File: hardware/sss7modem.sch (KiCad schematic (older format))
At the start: 30 parts, among them IC1 MCP2551-I/SN, IC2 LTV-352T, IC3 LTV-352T, K1 CONN_3, P1 CONN_4, U1 SIM1-0505, U2 74HCT125

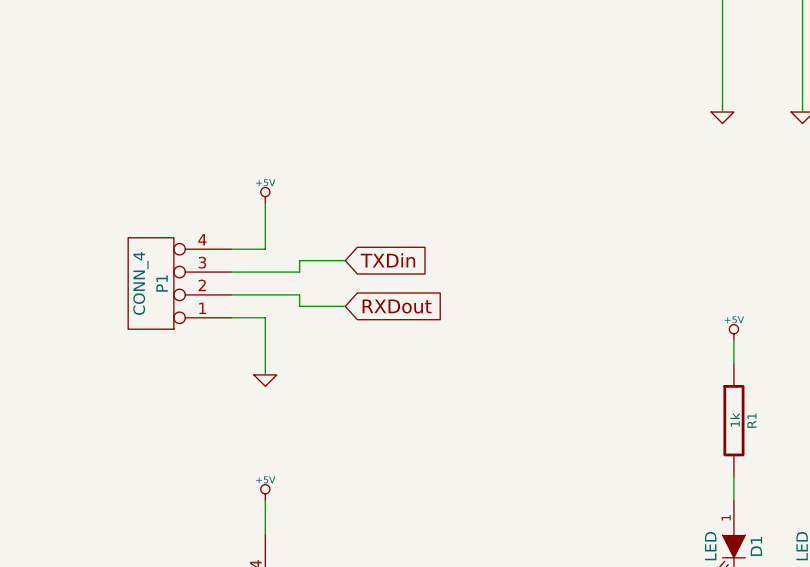
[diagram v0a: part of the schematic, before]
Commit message: First draft for the split ground pcb
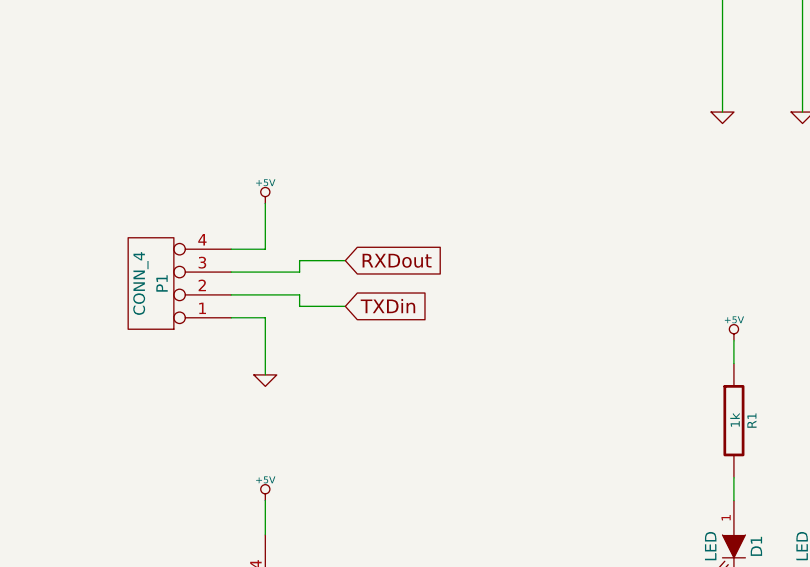
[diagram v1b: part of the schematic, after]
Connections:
- net RXDout: now also P1.3 (P3); no longer P1.2 (P2)
- net TXDin: now also P1.2 (P2); no longer P1.3 (P3)
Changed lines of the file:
@@
 Wire Wire Line
 	2900 3600 3100 3600
+Text GLabel 3100 3600 2    60   Input ~ 0
+TXDin
 Text GLabel 3100 3400 2    60   Input ~ 0
-TXDin
-Text GLabel 3100 3600 2    60   Input ~ 0
 RXDout
 Text Notes 7550 900  0    197  ~ 0

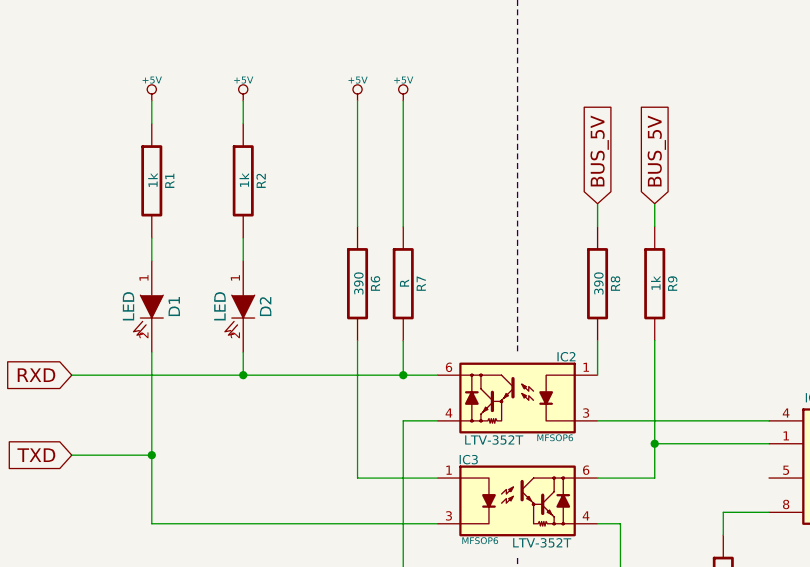
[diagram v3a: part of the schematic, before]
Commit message: Added missing resistor value
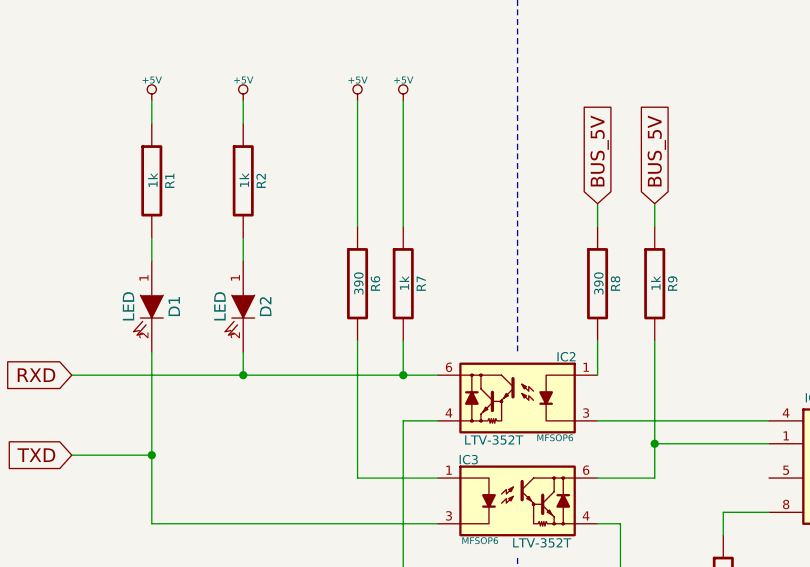
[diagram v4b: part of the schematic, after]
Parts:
- R7: value R -> 1k
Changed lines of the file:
@@
 Sheet 1 1
 Title "Seidenstrasse Signaling System 7 Modem"
-Date "26 may 2015"
+Date "22 jun 2015"
 Rev "1.0"
-Comp "Telebørken"
+Comp "Chaos Seidenstrasse Werke Kaiserslautern"
 Comment1 ""
 Comment2 ""
@@
 P 5900 4550
 F 0 "R7" V 5980 4550 40  0000 C CNN
-F 1 "R" V 5907 4551 40  0000 C CNN
+F 1 "1k" V 5907 4551 40  0000 C CNN
 F 2 "~" V 5830 4550 30  0000 C CNN
 F 3 "~" H 5900 4550 30  0000 C CNN

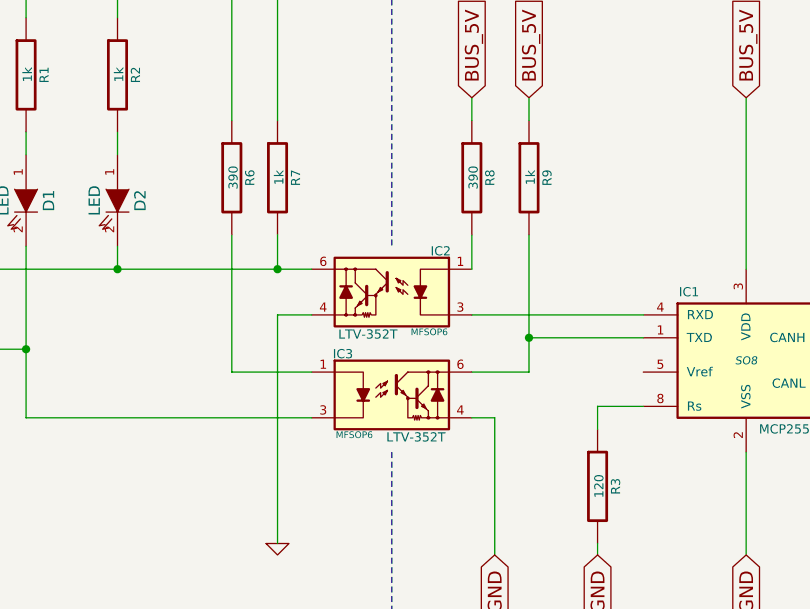
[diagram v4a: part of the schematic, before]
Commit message: Changes optocouplers to something faster. fixes #1
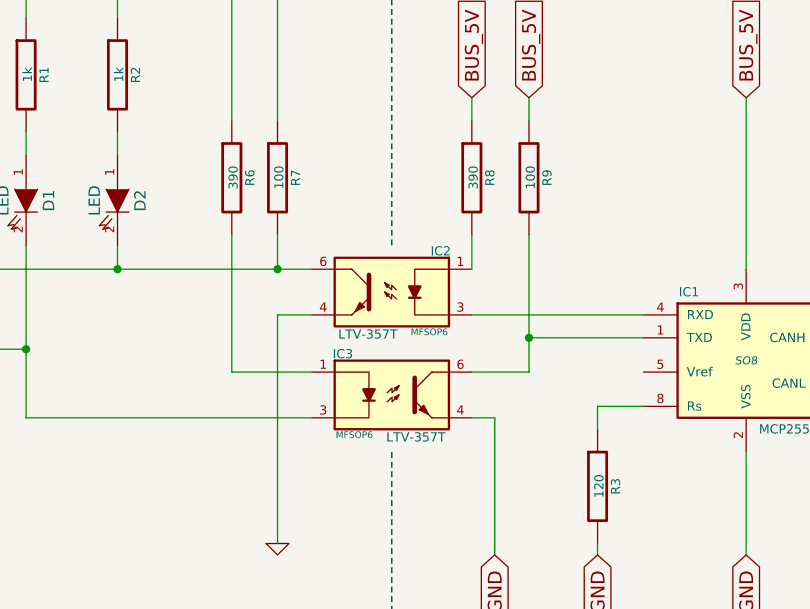
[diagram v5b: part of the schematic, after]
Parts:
- removed IC2, IC3: LTV-352T, MFSOP6, symbol LTV-352T
- added IC2, IC3: LTV-357T, MFSOP6, symbol LTV-357T
- R7, R9: value 1k -> 100
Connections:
- net BUS_GND: now also IC3.4
- net GND: now also IC2.4
- net RXD: now also IC2.6
- net TXD: now also IC3.3
- net at IC1.1 (TXD), R9.2: now also IC3.6
- net at IC1.4 (RXD): now also IC2.3
- net at R6.2: now also IC3.1
- net at R8.2: now also IC2.1
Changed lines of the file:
@@
 Sheet 1 1
 Title "Seidenstrasse Signaling System 7 Modem"
-Date "22 jun 2015"
+Date "8 jul 2015"
 Rev "1.0"
 Comp "Chaos Seidenstrasse Werke Kaiserslautern"
@@
 	1    0    0    -1
 $EndComp
-$Comp
-L LTV-352T IC3
-U 1 1 555DB3D8
-P 6400 5500
-F 0 "IC3" H 6186 5679 40  0000 C CNN
-F 1 "LTV-352T" H 6505 5315 40  0000 C CNN
-F 2 "MFSOP6" H 6236 5325 29  0000 C CNN
-F 3 "~" H 6400 5500 60  0000 C CNN
-	1    6400 5500
-	1    0    0    -1
-$EndComp
-$Comp
-L LTV-352T IC2
-U 1 1 555DB3E7
-P 6400 5050
-F 0 "IC2" H 6186 5229 40  0000 C CNN
-F 1 "LTV-352T" H 6505 4865 40  0000 C CNN
-F 2 "MFSOP6" H 6236 4875 29  0000 C CNN
-F 3 "~" H 6400 5050 60  0000 C CNN
-	1    6400 5050
-	-1   0    0    -1
-$EndComp
 Text GLabel 7950 4200 1    60   Input ~ 0
 BUS_5V
@@
 P 7000 4550
 F 0 "R9" V 7080 4550 40  0000 C CNN
-F 1 "1k" V 7007 4551 40  0000 C CNN
+F 1 "100" V 7007 4551 40  0000 C CNN
 F 2 "~" V 6930 4550 30  0000 C CNN
 F 3 "~" H 7000 4550 30  0000 C CNN
@@
 P 5900 4550
 F 0 "R7" V 5980 4550 40  0000 C CNN
-F 1 "1k" V 5907 4551 40  0000 C CNN
+F 1 "100" V 5907 4551 40  0000 C CNN
 F 2 "~" V 5830 4550 30  0000 C CNN
 F 3 "~" H 5900 4550 30  0000 C CNN
@@
 EndData
 $EndBitmap
+$Comp
+L LTV-357T IC3
+U 1 1 559CDFCD
+P 6400 5500
+F 0 "IC3" H 6186 5679 40  0000 C CNN
+F 1 "LTV-357T" H 6505 5315 40  0000 C CNN
+F 2 "MFSOP6" H 6236 5325 29  0000 C CNN
+F 3 "~" H 6400 5500 60  0000 C CNN
+	1    6400 5500
+	1    0    0    -1
+$EndComp
+$Comp
+L LTV-357T IC2
+U 1 1 559CDFF5
+P 6400 5050
+F 0 "IC2" H 6186 5229 40  0000 C CNN
+F 1 "LTV-357T" H 6505 4865 40  0000 C CNN
+F 2 "MFSOP6" H 6236 4875 29  0000 C CNN
+F 3 "~" H 6400 5050 60  0000 C CNN
+	1    6400 5050
+	-1   0    0    -1
+$EndComp
 $EndSCHEMATC

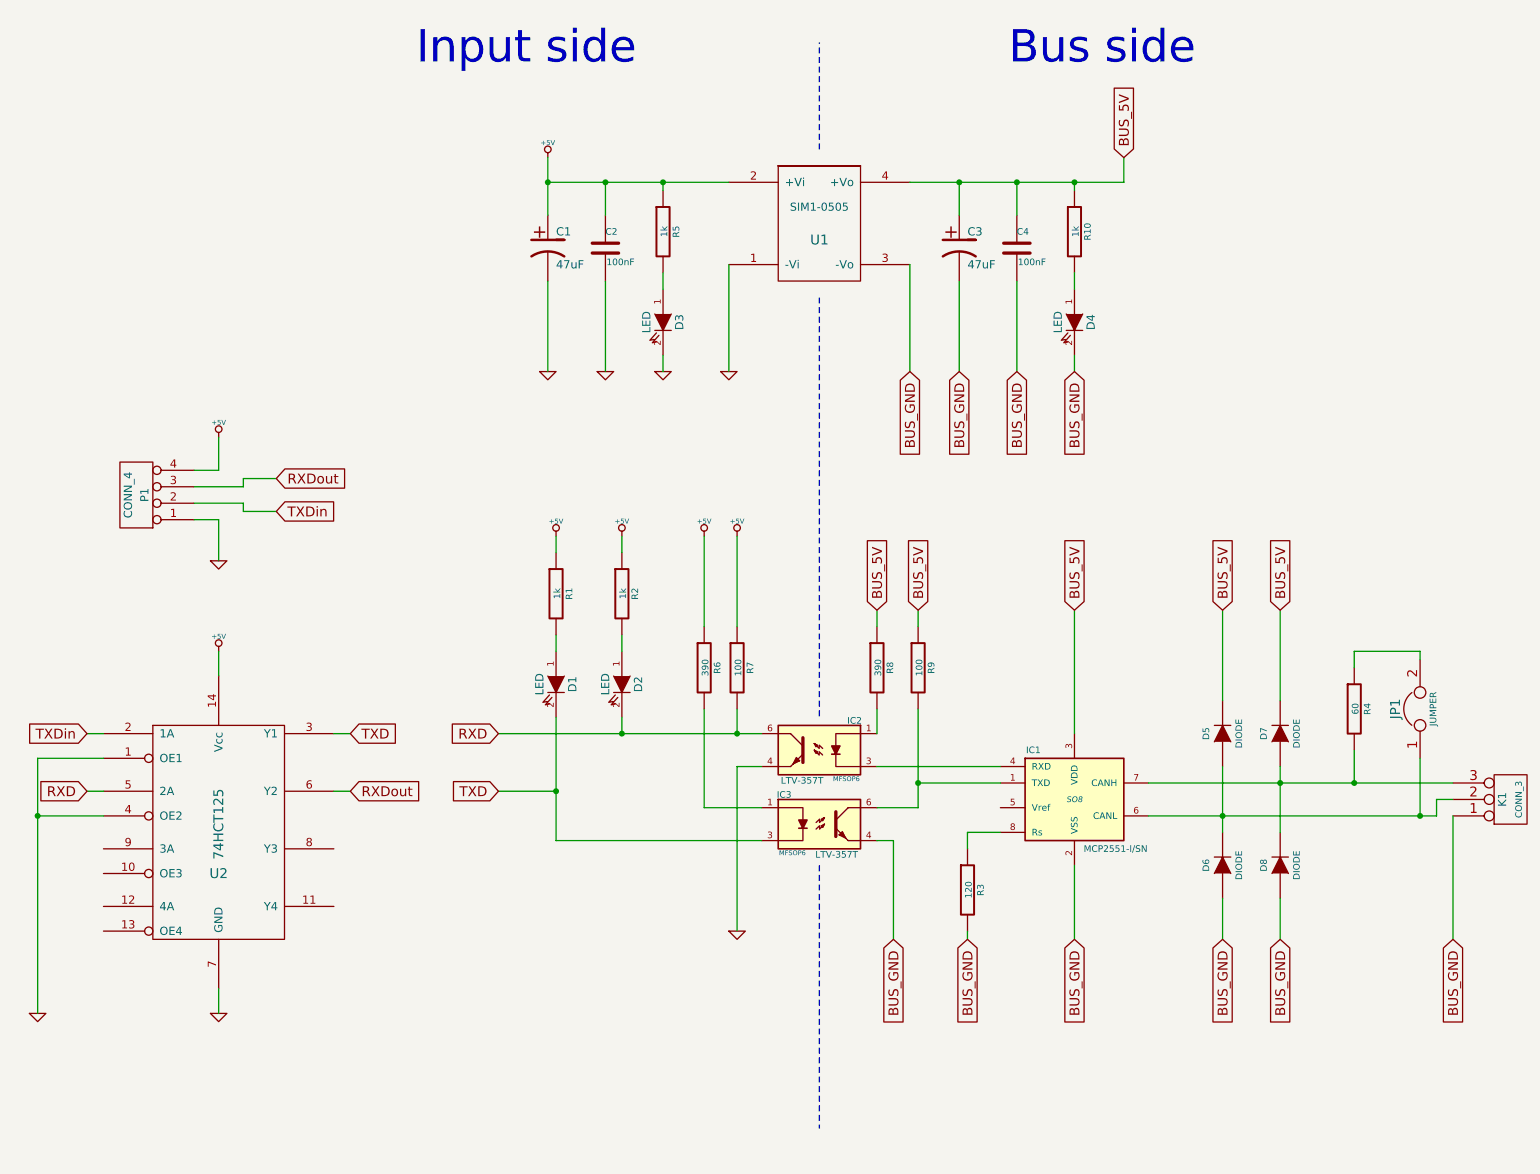
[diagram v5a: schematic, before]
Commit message: Fixed resistor values
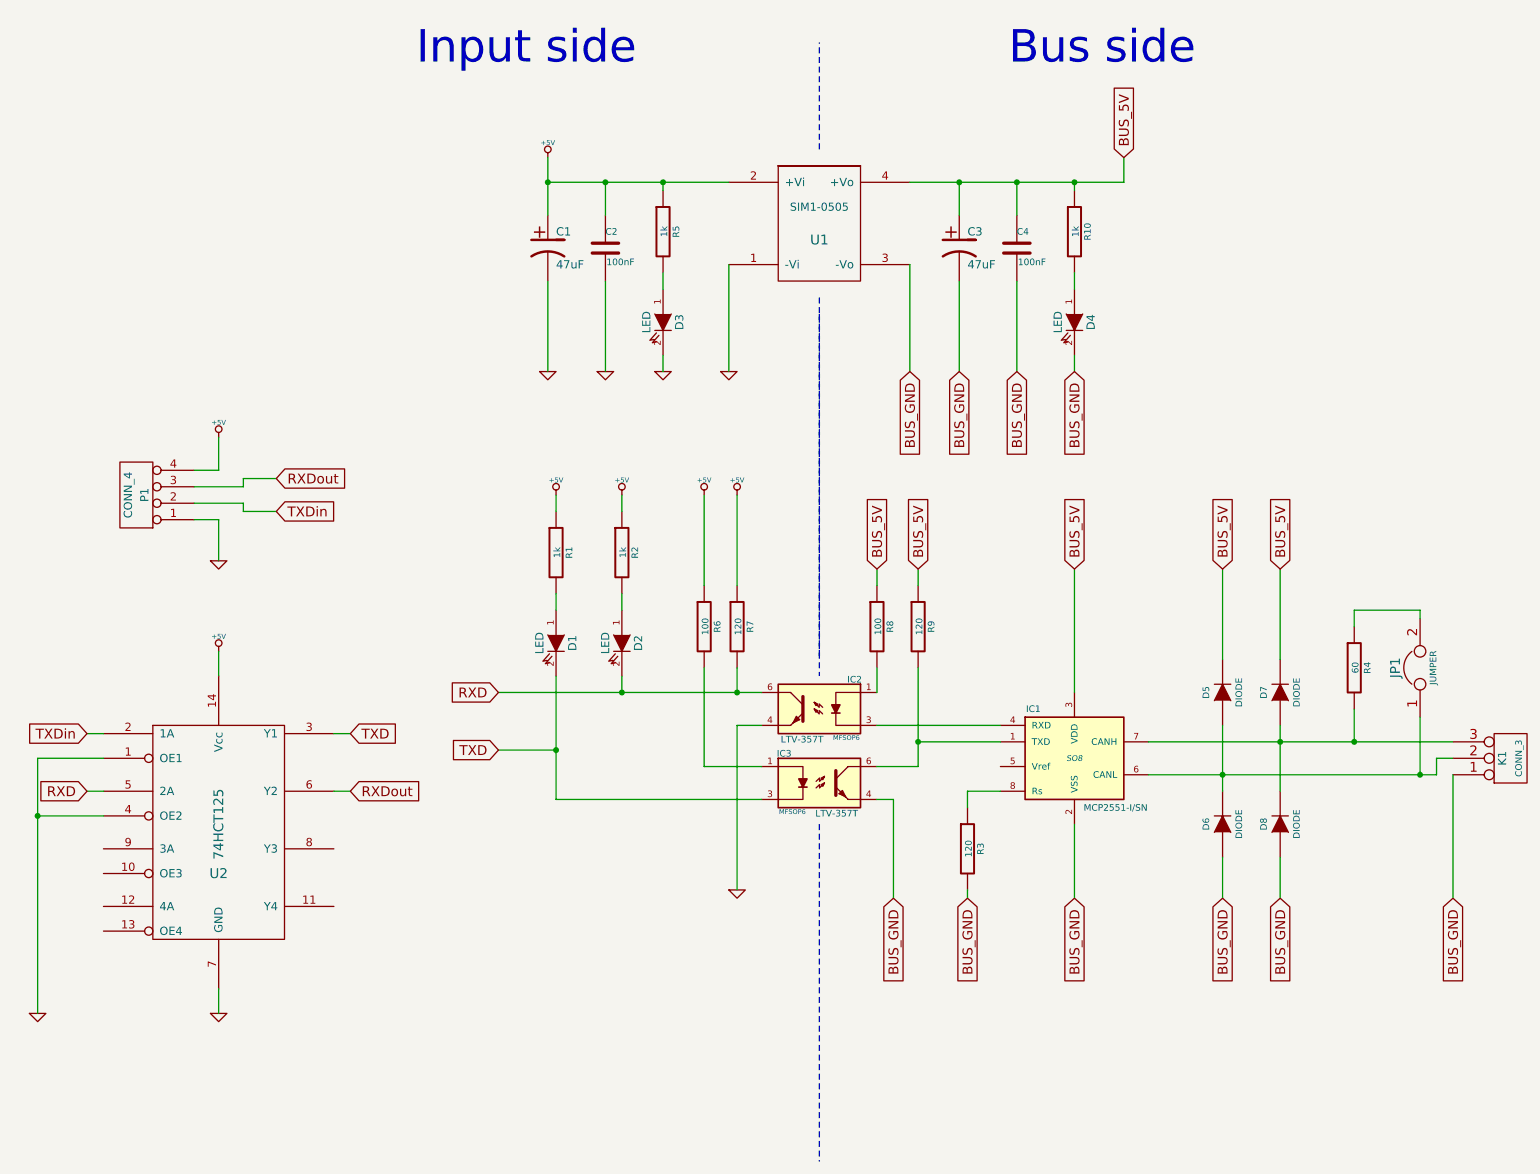
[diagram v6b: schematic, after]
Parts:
- R6, R8: value 390 -> 100
- R7, R9: value 100 -> 120
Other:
- moved on the sheet: D1, D2, D5, D6, D7, D8, IC1, IC2, IC3, JP1, K1, R1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

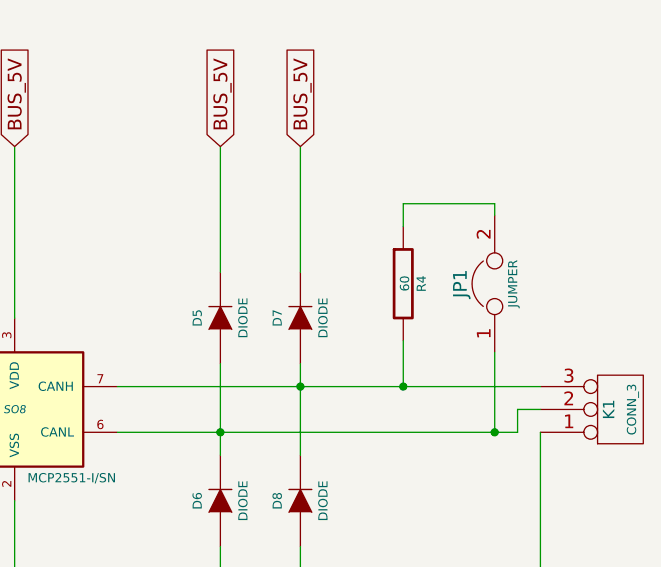
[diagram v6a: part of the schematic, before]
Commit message: Adjusted termination resistor and rebuild gerbers
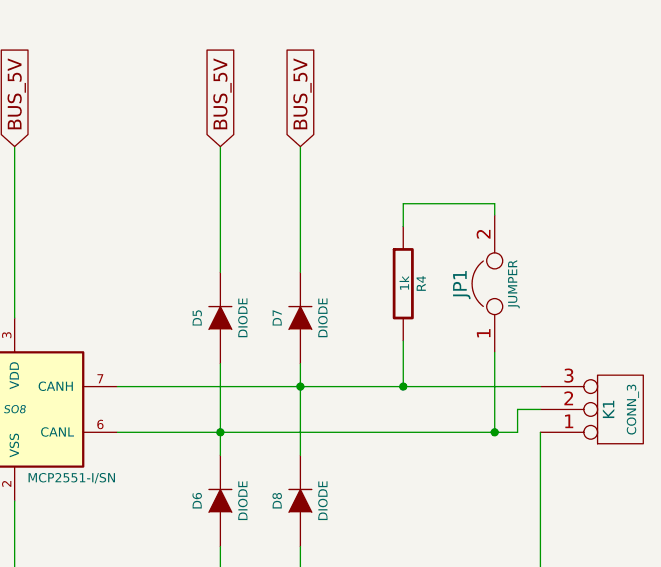
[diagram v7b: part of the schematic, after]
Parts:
- R4: value 60 -> 1k
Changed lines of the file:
@@
 P 9650 4550
 F 0 "R4" V 9730 4550 40  0000 C CNN
-F 1 "60" V 9657 4551 40  0000 C CNN
+F 1 "1k" V 9657 4551 40  0000 C CNN
 F 2 "~" V 9580 4550 30  0000 C CNN
 F 3 "~" H 9650 4550 30  0000 C CNN
